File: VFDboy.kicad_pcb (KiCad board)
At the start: 2 copper layers, 139.5 x 60 mm, 119 parts, among them J1 AVR-ISP-6, J2 USB_C_Receptacle_USB2.0, J3 Micro_SD_Card_Det, J4 TagConnect_TC2030_SWD, Q1 FS8205A, Q2 S9015, Q3 AO3401A, Q4 AO3401A, Q5 S9015, Q6 2N7002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

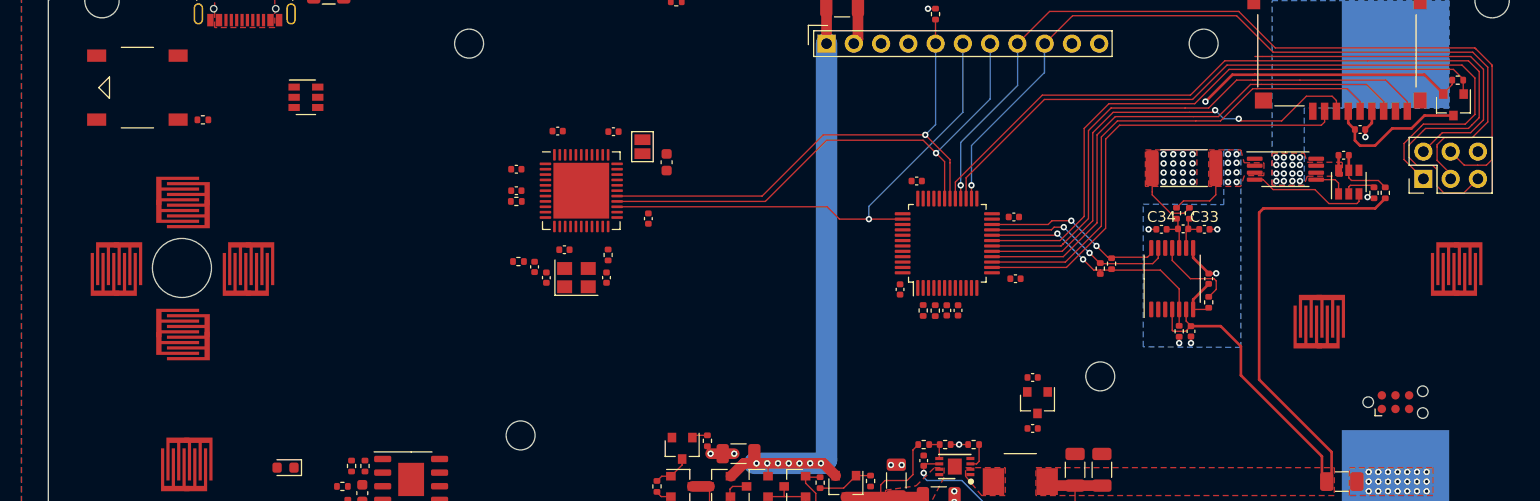
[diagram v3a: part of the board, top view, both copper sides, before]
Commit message: Connect buttons
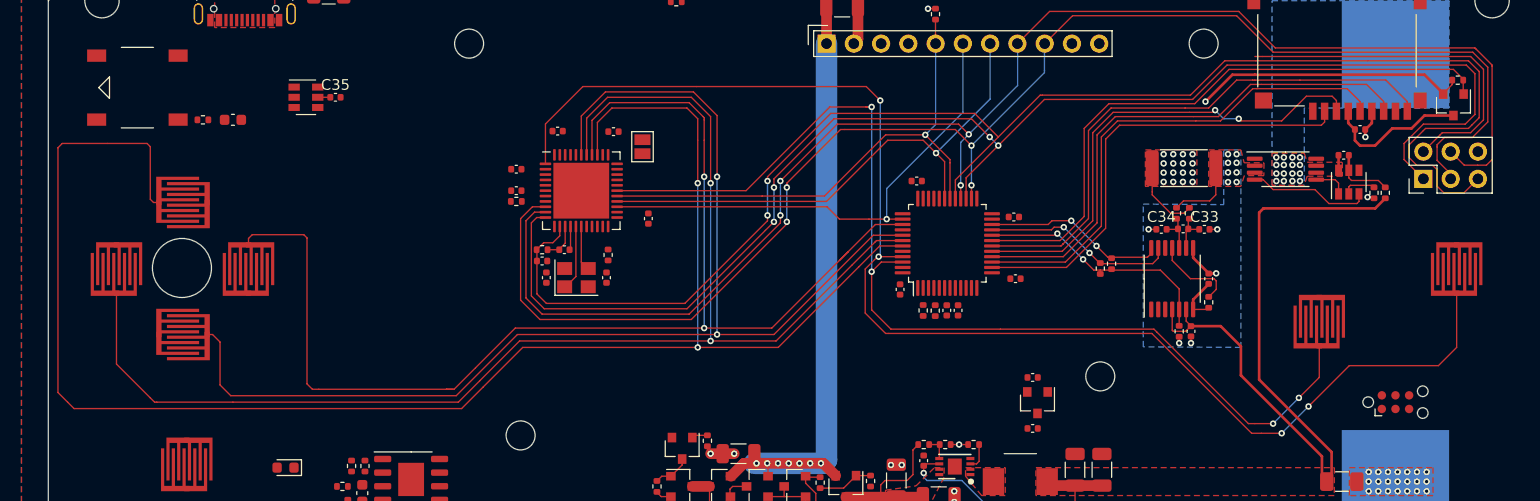
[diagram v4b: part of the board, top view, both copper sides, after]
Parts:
- added C35: 100nF, Capacitor_SMD:C_0402_1005Metric, F.Cu at (129.2, 114.0)
- moved C10 40.6 mm to (119.7, 116.1), turned to 0 degrees
- moved R1 2.46 mm to (148.5, 128.2), turned to 180 degrees
- moved C3 0.89 mm to (148.5, 129.2), turned to 180 degrees
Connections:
- U8 pad 45: /B -> /A
- U8 pad 46: /A -> /B
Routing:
- net /UP: track 0.00 -> 157.7 mm, vias 0 -> 2
- net /A: track 0.00 -> 127.8 mm, vias 0 -> 4
- net /LEFT: track 0.00 -> 125.0 mm, vias 0 -> 2
- net /RIGHT: track 0.00 -> 118.2 mm, vias 0 -> 2
- net /DOWN: track 0.00 -> 114.2 mm, vias 0 -> 2
- net /B: track 0.00 -> 100.2 mm, vias 0 -> 4
- net /SCK: track 76.0 -> 139.3 mm, vias 1 -> 4
- net /MISO: track 69.3 -> 132.6 mm, vias 0 -> 4
- net /~RST: track 77.7 -> 139.5 mm, vias 0 -> 2
- net /MOSI: track 77.6 -> 138.8 mm, vias 1 -> 4
- net Net-(C2-Pad1): track 0.00 -> 6.11 mm
- net +5V: track 95.5 -> 100.2 mm
- net Net-(C1-Pad2): track 0.00 -> 4.16 mm
- net GND: track 19.8 -> 22.1 mm
- net /~DC: track 47.1 -> 46.4 mm

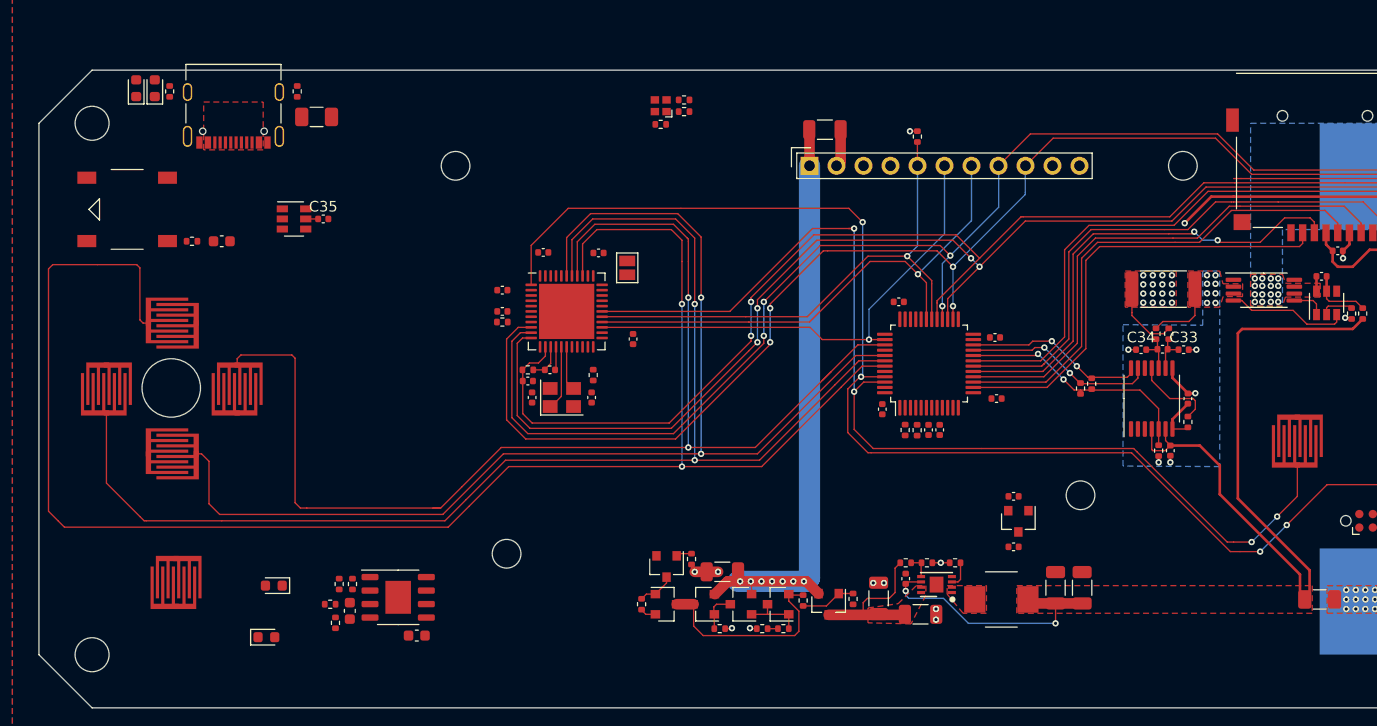
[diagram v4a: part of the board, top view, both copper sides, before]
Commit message: Route VBUS
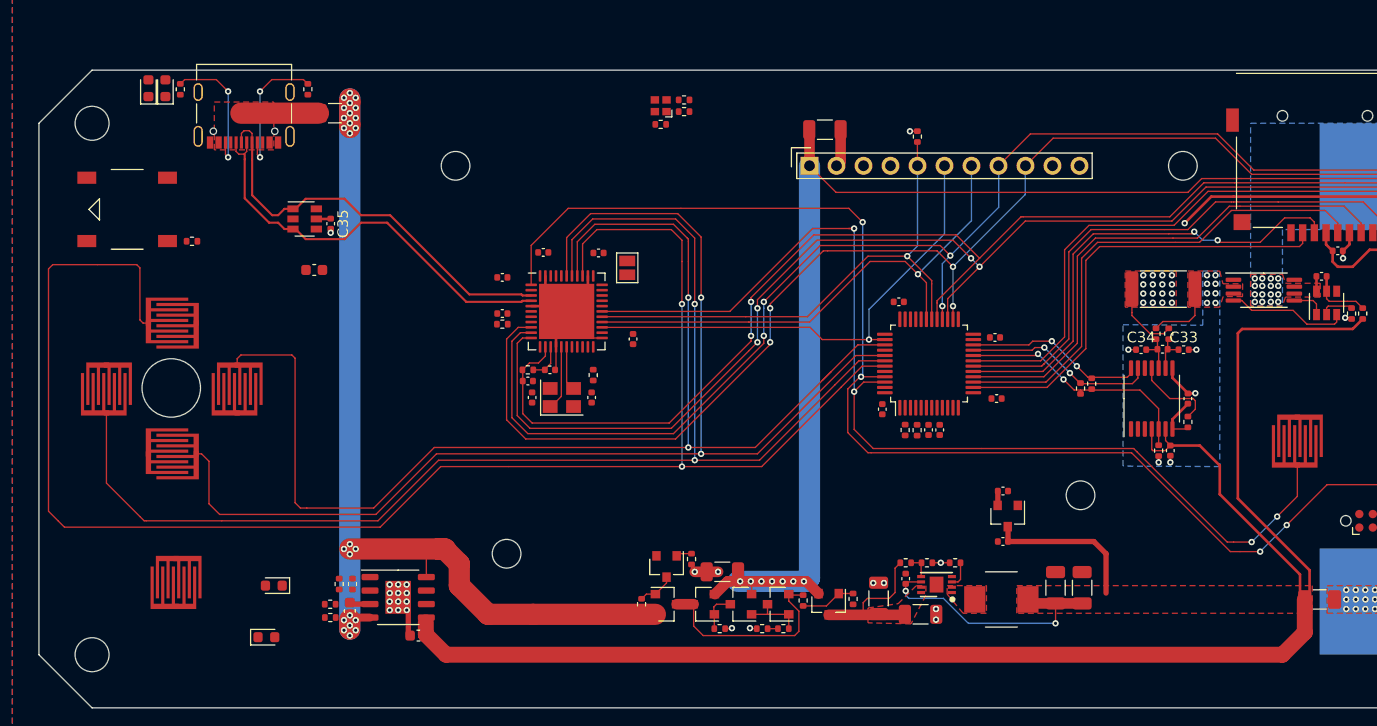
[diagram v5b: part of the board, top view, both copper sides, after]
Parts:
- moved C10 9.11 mm to (128.4, 118.8)
- moved F1 1.76 mm to (130.3, 104.0)
- moved C5 1.20 mm to (146.1, 119.5)
- moved D2 1.15 mm to (112.8, 101.7)
- moved C16 1.12 mm to (193.2, 144.3)
- moved C17 1.12 mm to (193.2, 139.6)
- moved U4 1.12 mm to (193.7, 141.9)
- moved R7 1.02 mm to (127.8, 101.8)
- moved R8 1.02 mm to (115.8, 101.8)
- moved D1 1.00 mm to (114.4, 101.7)
- moved J2 1.00 mm to (121.8, 104.3)
- moved U7 1.00 mm to (127.5, 114.0)
- moved C35 0.83 mm to (129.9, 114.5), turned to 270 degrees
- moved R14 0.70 mm to (129.9, 151.5), turned to 180 degrees
- moved C4 0.20 mm to (146.1, 122.9)
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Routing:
- net +BATT: track 95.0 -> 198.5 mm
- net VBUS: track 1.47 -> 92.8 mm, vias 0 -> 24
- net +5V: track 100.2 -> 141.7 mm
- net /D+: track 0.00 -> 39.4 mm
- net /D-: track 0.00 -> 39.1 mm
- net GND: track 22.1 -> 37.2 mm, vias 27 -> 40
- net Net-(J2-PadB5): track 0.00 -> 12.8 mm, vias 0 -> 2
- net Net-(J2-PadA5): track 0.00 -> 12.8 mm, vias 0 -> 2
- net Net-(F1-Pad2): track 0.00 -> 7.30 mm
- net +3V3: track 25.6 -> 27.0 mm
- net /RIGHT: track 118.2 -> 117.6 mm

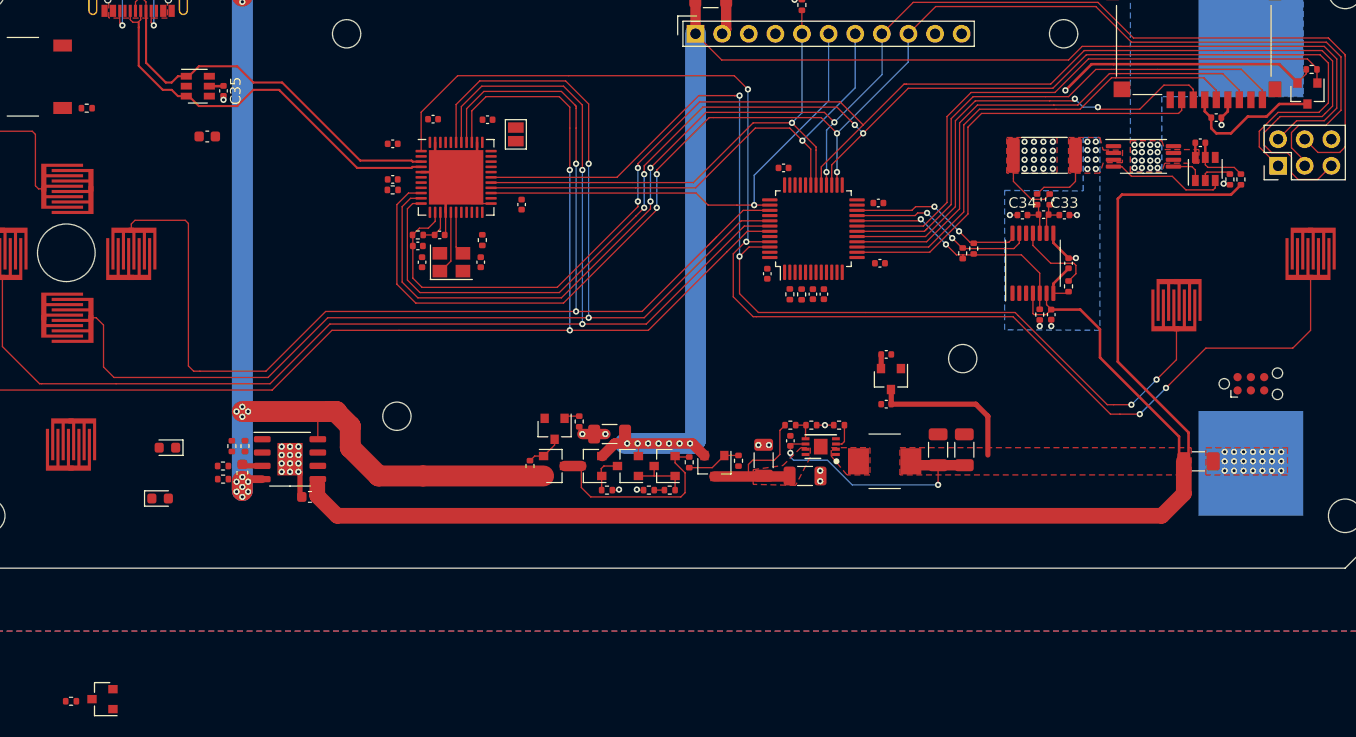
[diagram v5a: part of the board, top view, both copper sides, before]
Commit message: Route charger controls
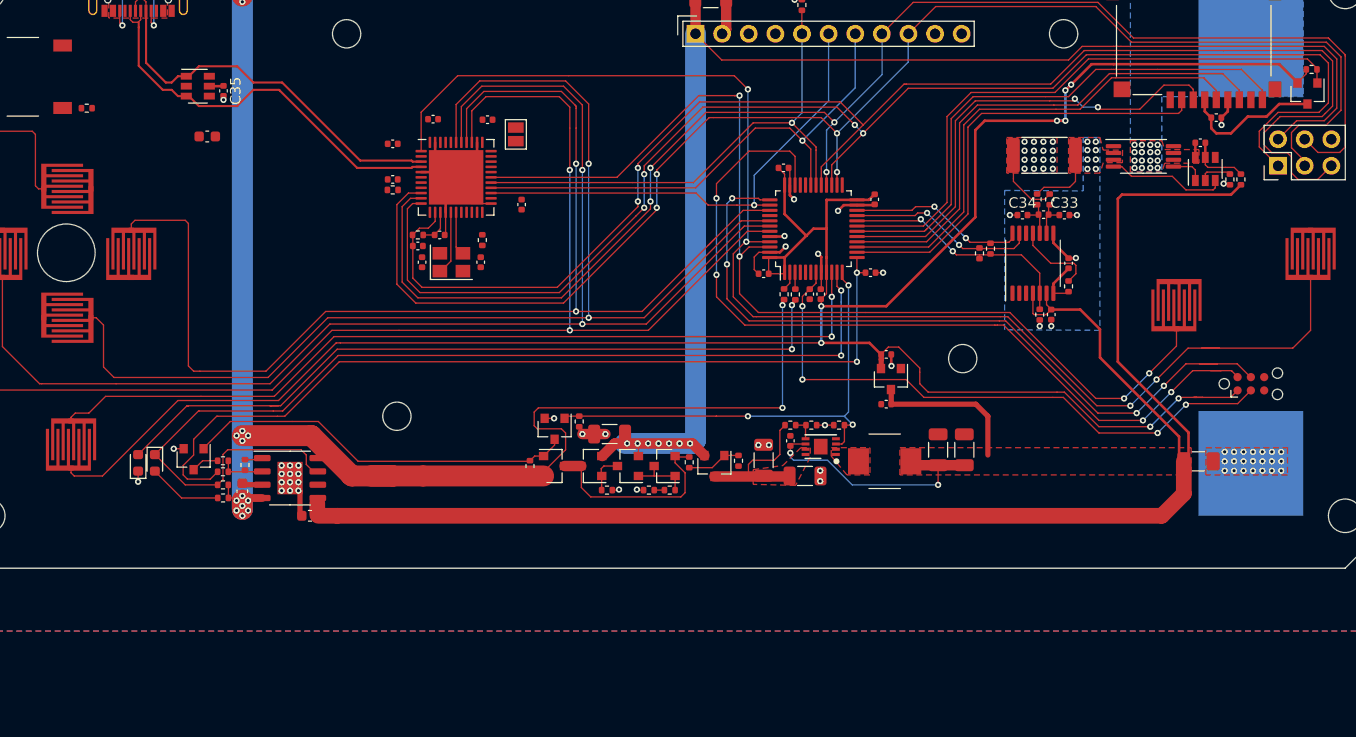
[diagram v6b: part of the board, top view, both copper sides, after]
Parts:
- moved R26 27.1 mm to (129.9, 149.8), turned to 180 degrees
- moved Q8 24.5 mm to (127.1, 149.6), turned to 270 degrees
- moved D4 3.44 mm to (123.4, 149.9), turned to 270 degrees
- moved D5 3.15 mm to (121.8, 149.9), turned to 90 degrees
- moved R36 2.59 mm to (129.9, 150.8), turned to 0 degrees
- moved C19 1.80 mm to (131.8, 152.7)
- moved C26 1.80 mm to (138.2, 155.0)
- moved R14 1.80 mm to (129.9, 153.3)
- moved R15 1.80 mm to (132.0, 150.2)
- moved R27 1.80 mm to (129.9, 152.1)
- moved U6 1.80 mm to (136.3, 151.4)
- moved R33 1.60 mm to (203.2, 129.5)
- moved R34 1.60 mm to (202.1, 129.9)
- moved C30 1.27 mm to (191.7, 131.8)
- moved R25 0.60 mm to (184.5, 133.9)
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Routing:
- net +3V3: track 27.0 -> 228.9 mm, vias 1 -> 8
- net /Power/LEDchg: track 0.00 -> 98.5 mm, vias 0 -> 2
- net /Power/Ichg: track 0.00 -> 84.7 mm, vias 0 -> 2
- net Net-(SW8-Pad1): track 0.00 -> 82.3 mm, vias 0 -> 2
- net Net-(J4-Pad2): track 0.00 -> 80.3 mm, vias 0 -> 4
- net Net-(D5-Pad2): track 0.00 -> 72.3 mm, vias 0 -> 2
- net Net-(J4-Pad4): track 0.00 -> 72.1 mm, vias 0 -> 4
- net /STM32/~STMRST: track 0.00 -> 57.4 mm, vias 0 -> 4
- net VBUS: track 92.8 -> 140.8 mm, vias 24 -> 26
- net /Power/PWR_EN: track 3.87 -> 45.3 mm, vias 0 -> 3
- net /Power/~PWR_EN: track 3.52 -> 37.4 mm
- net GND: track 37.2 -> 60.4 mm, vias 40 -> 50
- net Net-(D4-Pad2): track 0.00 -> 7.06 mm
- net Net-(R15-Pad1): track 0.00 -> 4.28 mm
- net Net-(Q8-Pad3): track 0.00 -> 2.74 mm
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
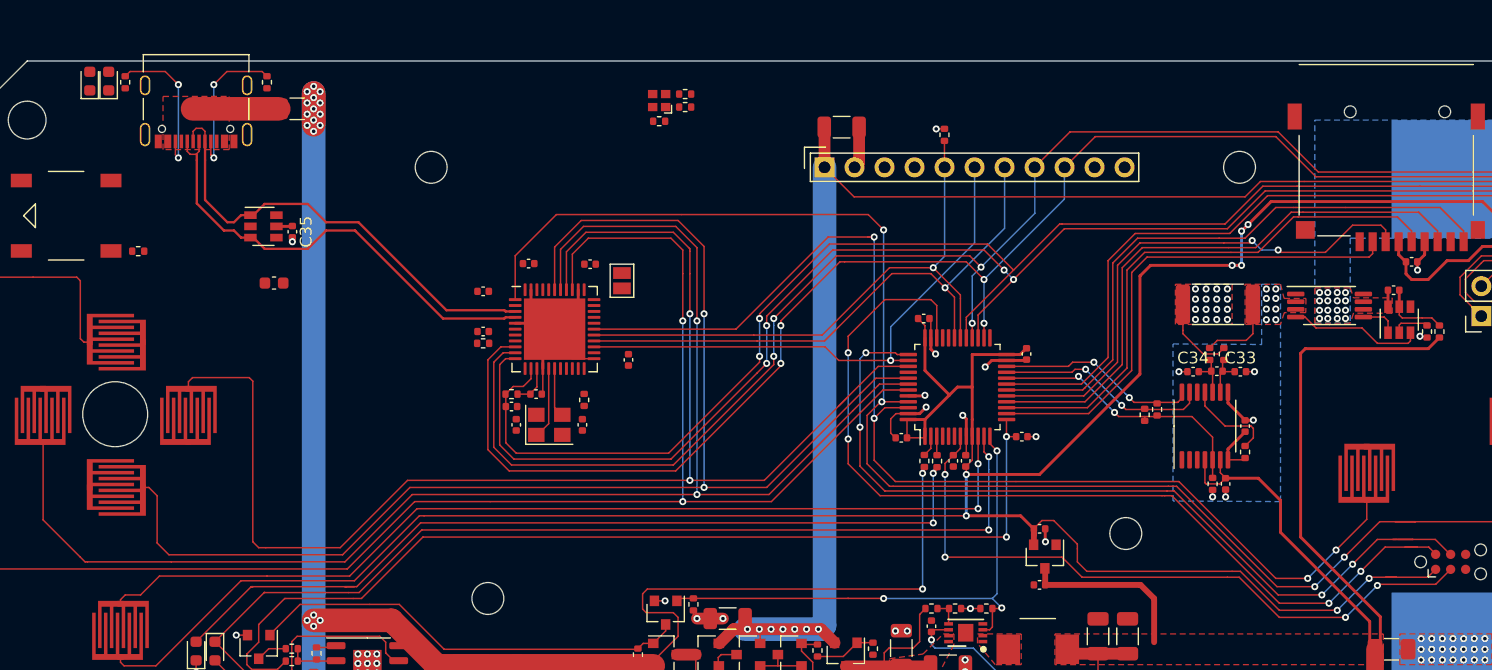
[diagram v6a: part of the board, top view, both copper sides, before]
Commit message: route RGB LED
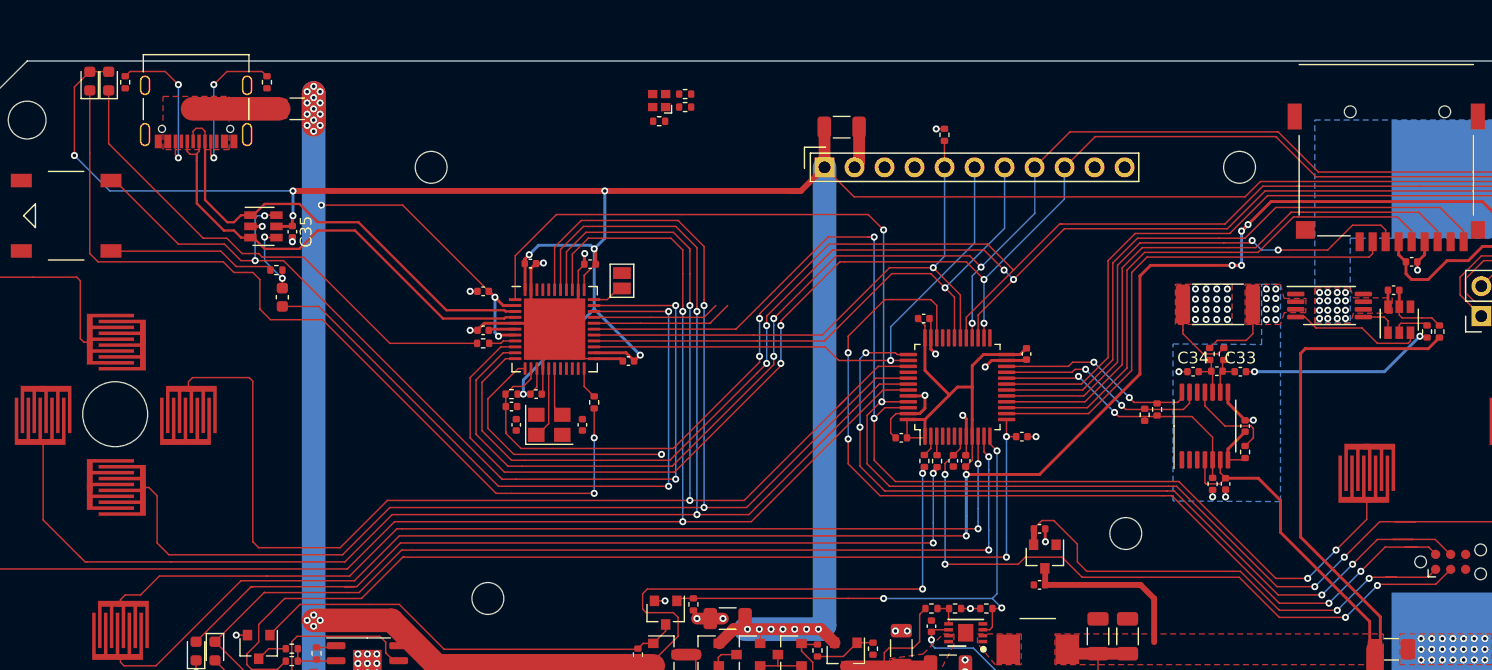
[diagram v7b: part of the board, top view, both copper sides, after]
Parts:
- moved R21 11.8 mm to (128.6, 117.7)
- moved C10 1.39 mm to (129.1, 120.0), turned to 270 degrees
- moved R6 0.88 mm to (155.5, 128.9)
- moved C6 0.15 mm to (150.1, 117.2)
- moved C4 0.10 mm to (146.1, 122.8)
- moved C7 0.10 mm to (158.4, 125.4), turned to 0 degrees
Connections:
- C20 pad 1: Net-(C20-Pad1) -> /STM32/SD_PWR
- J3 pad 4: Net-(C20-Pad1) -> /STM32/SD_PWR
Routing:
- net +5V: track 141.7 -> 263.5 mm, vias 7 -> 15
- net /SPKR-: track 0.00 -> 85.4 mm, vias 0 -> 4
- net Net-(D2-Pad1): track 0.00 -> 73.6 mm, vias 0 -> 2
- net Net-(C10-Pad2): track 0.00 -> 60.2 mm, vias 0 -> 2
- net Net-(D1-Pad1): track 0.00 -> 42.7 mm
- net VBUS: track 140.8 -> 165.7 mm, vias 26 -> 29
- net Net-(R4-Pad2): track 0.00 -> 22.3 mm, vias 0 -> 1
- net GND: track 60.4 -> 76.0 mm, vias 50 -> 54
- net GNDREF: track 13.6 -> 28.8 mm
- net Net-(LS1-Pad1): track 0.00 -> 14.3 mm
- net Net-(C20-Pad1): track 13.5 -> 0.00 mm
- net /STM32/SD_PWR: track 0.00 -> 13.5 mm
- net Net-(R2-Pad2): track 0.00 -> 11.9 mm
- net Net-(R3-Pad2): track 0.00 -> 10.7 mm
- net /SPKR+: track 0.00 -> 6.67 mm, vias 0 -> 2
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
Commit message: Finish layout
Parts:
- moved R4 12.4 mm to (161.2, 117.5), turned to 270 degrees
- moved D3 2.78 mm to (163.4, 104.8)
- moved R3 2.78 mm to (165.6, 104.2)
- moved R2 2.78 mm to (165.6, 105.3)
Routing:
- net Net-(R3-Pad2): track 10.7 -> 27.5 mm, vias 0 -> 2
- net Net-(R4-Pad2): track 22.3 -> 38.3 mm, vias 1 -> 2
- net Net-(R2-Pad2): track 11.9 -> 27.5 mm, vias 0 -> 2
- net Net-(D3-Pad2): track 0.00 -> 12.4 mm, vias 0 -> 2
- net +5V: track 263.5 -> 274.9 mm
- net GND: track 76.0 -> 84.0 mm, vias 54 -> 62
- net Net-(Q1-Pad1): track 0.00 -> 7.32 mm
- net /A: track 128.8 -> 124.8 mm, vias 4 -> 2
- net Net-(J4-Pad2): track 80.3 -> 76.7 mm, vias 4 -> 2
- net /STM32/~STMRST: track 58.4 -> 55.5 mm, vias 4 -> 2
- net Net-(J4-Pad4): track 72.1 -> 69.6 mm, vias 4 -> 2
- net Net-(C2-Pad1): track 6.11 -> 8.01 mm
- net Net-(C1-Pad2): track 4.16 -> 5.76 mm
- net +3V3: track 223.2 -> 224.8 mm, vias 8 -> 6
- net Net-(D3-Pad4): track 0.00 -> 1.19 mm
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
